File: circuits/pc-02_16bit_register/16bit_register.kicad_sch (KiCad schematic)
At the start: 34 parts, among them J1 Conn_01x10, U1 74HC273, U2 74HC273, U3 74HC244, U4 74HC244, U5 74HC244, U6 74HC244

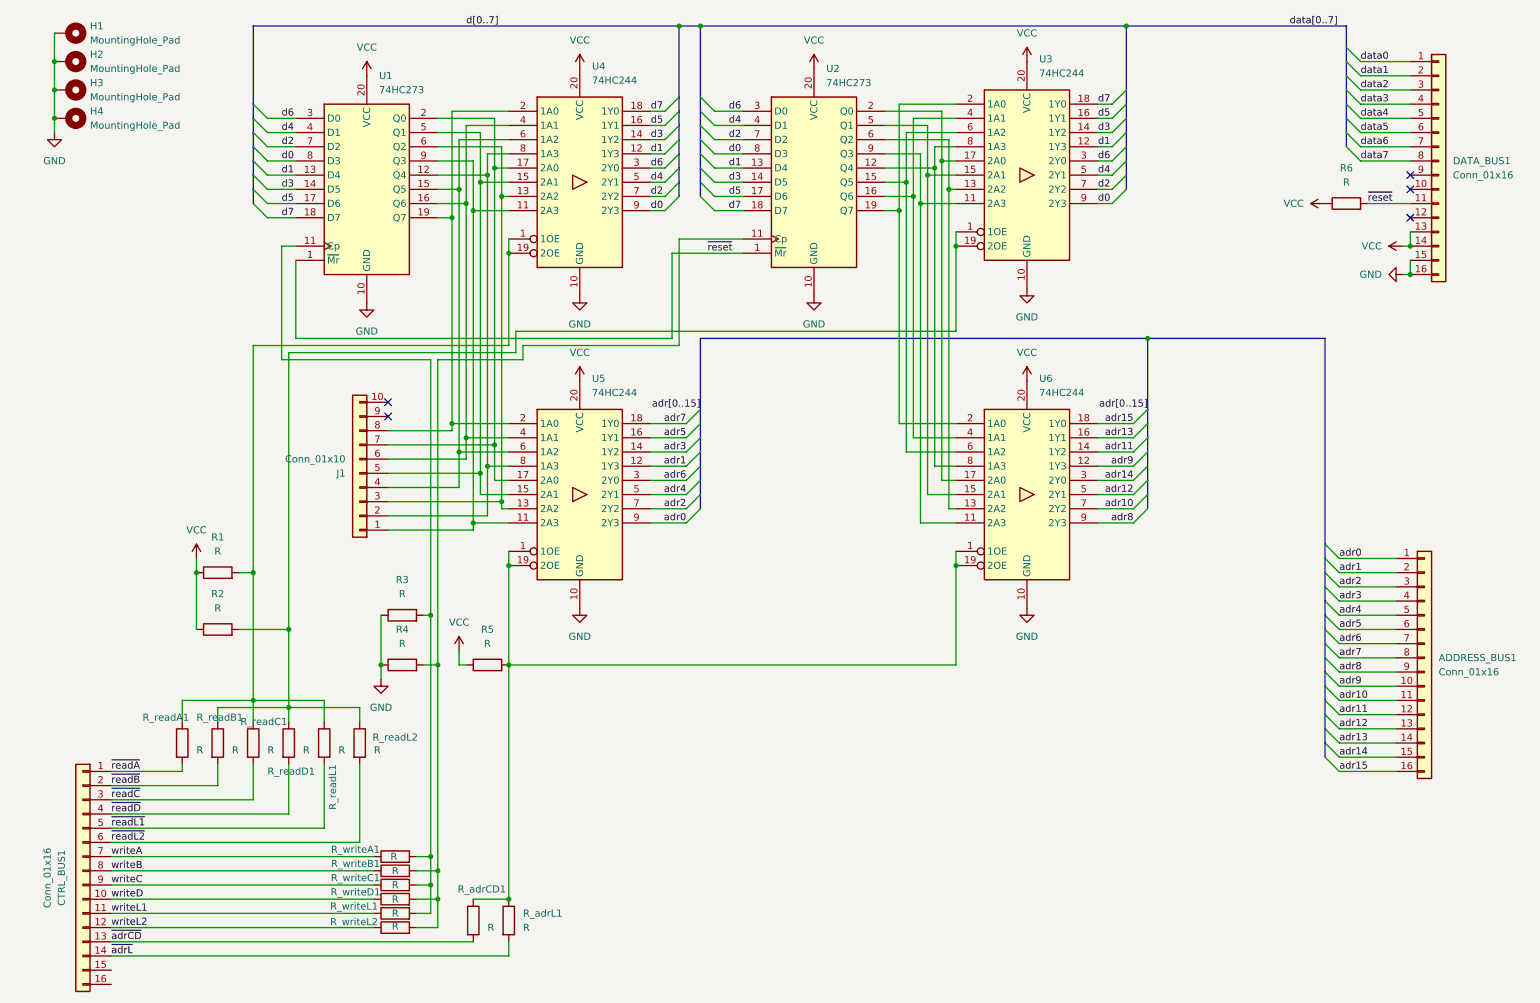
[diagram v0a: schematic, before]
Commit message: pc-02 rev A: 16bit register unit for PC and SP
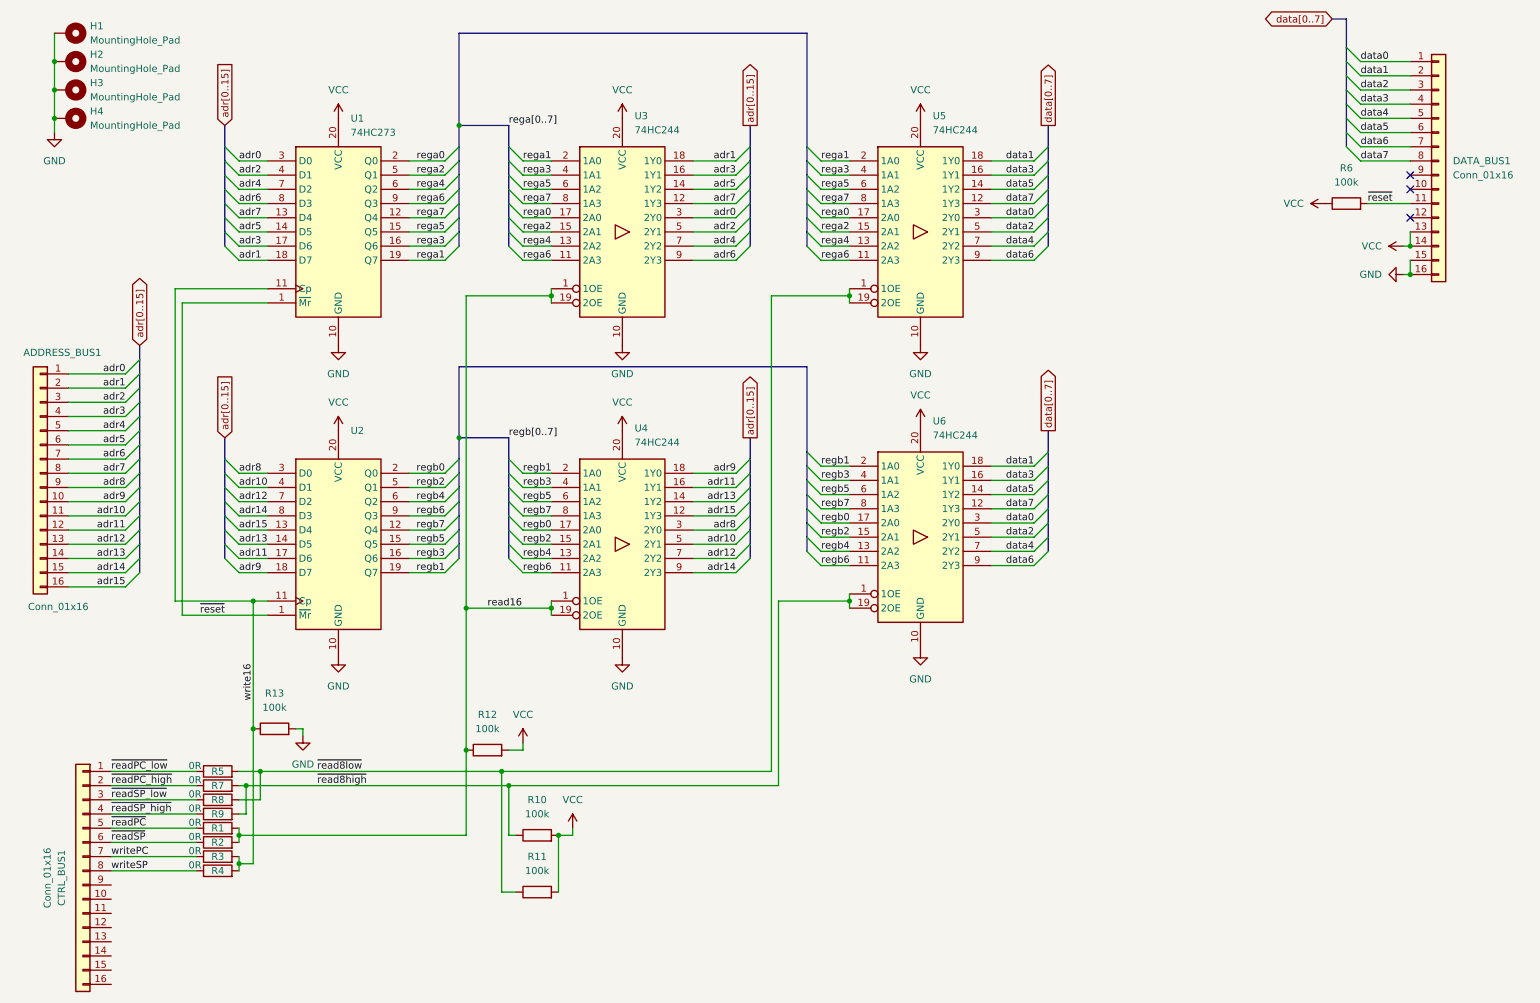
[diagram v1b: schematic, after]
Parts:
- removed J1: Conn_01x10, Connector_IDC:IDC-Header_2x05_P2.54mm_Horizontal, symbol Connector_Generic:Conn_01x10
- removed R_adrCD1, R_adrL1, R_readA1, R_readB1, R_readC1, R_readD1, R_readL1, R_readL2, R_writeA1, R_writeB1, R_writeC1, R_writeD1, R_writeL1, R_writeL2: R, Resistor_SMD:R_0603_1608Metric, symbol Device:R
- added R10, R11, R12, R13: 100k, Resistor_SMD:R_0603_1608Metric, symbol Device:R
- added R7, R8, R9: 0R, Resistor_SMD:R_0603_1608Metric, symbol Device:R
- R1, R2, R3, R4, R5: value R -> 0R
- R6: value R -> 100k
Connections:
- net GND: now also R13.2; no longer R3.1, R4.1
- net VCC: now also R10.2, R11.2, R12.2; no longer R1.1, R2.1, R5.1
- net adr0: now also U1.3 (D0), U3.3 (2Y0); no longer U5.9 (2Y3)
- net adr1: now also U1.18 (D7), U3.18 (1Y0); no longer U5.12 (1Y3)
- net adr10: now also U2.4 (D1), U4.5 (2Y1); no longer U6.7 (2Y2)
- net adr11: now also U2.17 (D6), U4.16 (1Y1); no longer U6.14 (1Y2)
- net adr12: now also U2.7 (D2), U4.7 (2Y2); no longer U6.5 (2Y1)
- net adr13: now also U2.14 (D5), U4.14 (1Y2); no longer U6.16 (1Y1)
- net adr14: now also U2.8 (D3), U4.9 (2Y3); no longer U6.3 (2Y0)
- net adr15: now also U2.13 (D4), U4.12 (1Y3); no longer U6.18 (1Y0)
- net adr2: now also U1.4 (D1), U3.5 (2Y1); no longer U5.7 (2Y2)
- net adr3: now also U1.17 (D6), U3.16 (1Y1); no longer U5.14 (1Y2)
- net adr4: now also U1.7 (D2), U3.7 (2Y2); no longer U5.5 (2Y1)
- net adr5: now also U1.14 (D5), U3.14 (1Y2); no longer U5.16 (1Y1)
- net adr6: now also U1.8 (D3), U3.9 (2Y3); no longer U5.3 (2Y0)
- net adr7: now also U1.13 (D4), U3.12 (1Y3); no longer U5.18 (1Y0)
- net adr8: now also U2.3 (D0), U4.3 (2Y0); no longer U6.9 (2Y3)
- net adr9: now also U2.18 (D7), U4.18 (1Y0); no longer U6.12 (1Y3)
- net data0: now also U5.3 (2Y0), U6.3 (2Y0)
- net data1: now also U5.18 (1Y0), U6.18 (1Y0)
- net data2: now also U5.5 (2Y1), U6.5 (2Y1)
- net data3: now also U5.16 (1Y1), U6.16 (1Y1)
- net data4: now also U5.7 (2Y2), U6.7 (2Y2)
- net data5: now also U5.14 (1Y2), U6.14 (1Y2)
- net data6: now also U5.9 (2Y3), U6.9 (2Y3)
- net data7: now also U5.12 (1Y3), U6.12 (1Y3)
- net write16: now reaches R3.2, U1.11 (Cp)
- net write16: now also R4.2, U2.11 (Cp), R13.1
- net rega7: now reaches U1.12 (Q4), U5.8 (1A3)
- net rega7: now also U3.8 (1A3); no longer U4.8 (1A3)
- net rega5: now reaches U1.15 (Q5), U5.6 (1A2)
- net rega5: now also U3.6 (1A2); no longer U4.6 (1A2)
- net rega3: now reaches U1.16 (Q6), U5.4 (1A1)
- net rega3: now also U3.4 (1A1); no longer U4.4 (1A1)
- net rega1: now reaches U1.19 (Q7), U5.2 (1A0)
- net rega1: now also U3.2 (1A0); no longer U4.2 (1A0)
- net rega0: now reaches U1.2 (Q0), U5.17 (2A0)
- net rega0: now also U3.17 (2A0); no longer U4.17 (2A0)
- net rega2: now reaches U1.5 (Q1), U5.15 (2A1)
- net rega2: now also U3.15 (2A1); no longer U4.15 (2A1)
- net rega4: now reaches U1.6 (Q2), U5.13 (2A2)
- net rega4: now also U3.13 (2A2); no longer U4.13 (2A2)
- net rega6: now reaches U1.9 (Q3), U5.11 (2A3)
- net rega6: now also U3.11 (2A3); no longer U4.11 (2A3)
- net ~{read8low}: now reaches R5.2, U5.1 (1OE), U5.19 (2OE)
- net ~{read8low}: now also R11.1, R8.2; no longer U6.1 (1OE), U6.19 (2OE)
- net read16: now reaches R2.2, U3.1 (1OE), U3.19 (2OE)
- net read16: now also R1.2, U4.1 (1OE), U4.19 (2OE), R12.1
- net regb7: now reaches U2.12 (Q4), U6.8 (1A3)
- net regb7: now also U4.8 (1A3); no longer U3.8 (1A3)
- net regb5: now reaches U2.15 (Q5), U6.6 (1A2)
- net regb5: now also U4.6 (1A2); no longer U3.6 (1A2)
- net regb3: now reaches U2.16 (Q6), U6.4 (1A1)
- net regb3: now also U4.4 (1A1); no longer U3.4 (1A1)
- net regb1: now reaches U2.19 (Q7), U6.2 (1A0)
- net regb1: now also U4.2 (1A0); no longer U3.2 (1A0)
- net regb0: now reaches U2.2 (Q0), U6.17 (2A0)
- net regb0: now also U4.17 (2A0); no longer U3.17 (2A0)
- net regb2: now reaches U2.5 (Q1), U6.15 (2A1)
- net regb2: now also U4.15 (2A1); no longer U3.15 (2A1)
- net regb4: now reaches U2.6 (Q2), U6.13 (2A2)
- net regb4: now also U4.13 (2A2); no longer U3.13 (2A2)
- net regb6: now reaches U2.9 (Q3), U6.11 (2A3)
- net regb6: now also U4.11 (2A3); no longer U3.11 (2A3)
- removed net d0: U1.8 (D3), U2.8 (D3), U3.9 (2Y3), U4.9 (2Y3)
- removed net d1: U1.13 (D4), U2.13 (D4), U3.12 (1Y3), U4.12 (1Y3)
- removed net d2: U1.7 (D2), U2.7 (D2), U3.7 (2Y2), U4.7 (2Y2)
- removed net d3: U1.14 (D5), U2.14 (D5), U3.14 (1Y2), U4.14 (1Y2)
- removed net d4: U1.4 (D1), U2.4 (D1), U3.5 (2Y1), U4.5 (2Y1)
- removed net d5: U1.17 (D6), U2.17 (D6), U3.16 (1Y1), U4.16 (1Y1)
- removed net d6: U1.3 (D0), U2.3 (D0), U3.3 (2Y0), U4.3 (2Y0)
- removed net d7: U1.18 (D7), U2.18 (D7), U3.18 (1Y0), U4.18 (1Y0)
- net writeA renamed writePC
- net writePC: now also R3.1
- net writeB renamed writeSP
- net writeSP: now also R4.1
- net writeC: no longer names the net of CTRL_BUS1.9 (Pin_9)
- net writeD: no longer names the net of CTRL_BUS1.10 (Pin_10)
- net writeL1: no longer names the net of CTRL_BUS1.11 (Pin_11)
- net writeL2: no longer names the net of CTRL_BUS1.12 (Pin_12)
- net ~{adrCD}: no longer names the net of CTRL_BUS1.13 (Pin_13)
- net ~{adrL}: no longer names the net of CTRL_BUS1.14 (Pin_14)
- net ~{readA} renamed ~{readPC_low}
- net ~{readPC_low}: now also R5.1
- net ~{readB} renamed ~{readPC_high}
- net ~{readPC_high}: now also R7.1
- net ~{readC} renamed ~{readSP_low}
- net ~{readSP_low}: now also R8.1
- net ~{readD} renamed ~{readSP_high}
- net ~{readSP_high}: now also R9.1
- net ~{readL1} renamed ~{readPC}
- net ~{readPC}: now also R1.1
- net ~{readL2} renamed ~{readSP}
- net ~{readSP}: now also R2.1
- new net ~{read8high}: R10.1, R7.2, R9.2, U6.1 (1OE), U6.19 (2OE)
- no-connect marks 5 -> 3
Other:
- title: PC-01 Dual Register Unit -> PC-02 16Bit Register Unit
- moved on the sheet: ADDRESS_BUS1, U1, U2, U3, U4, U5, U6

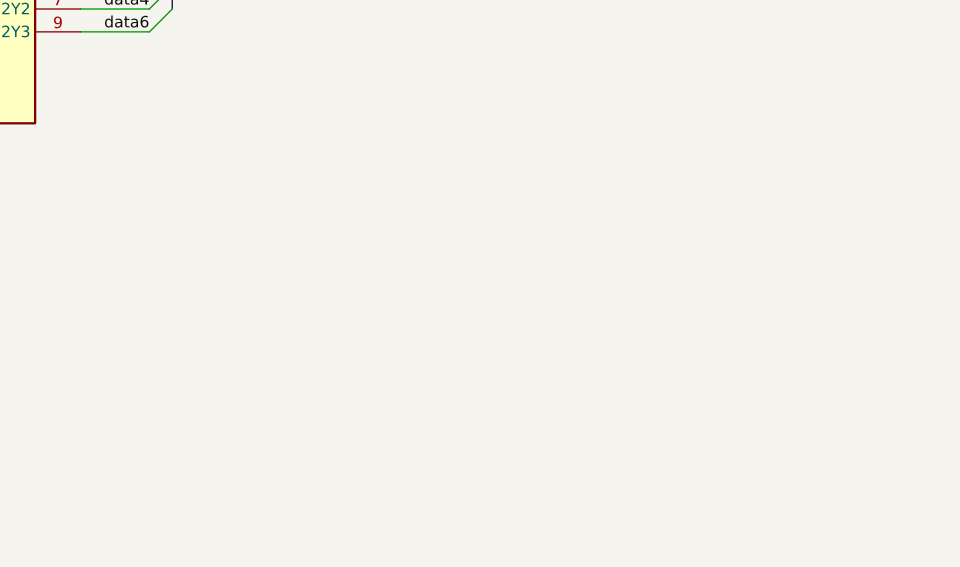
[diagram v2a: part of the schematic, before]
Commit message: add filter and decoupling capacitors to all boards
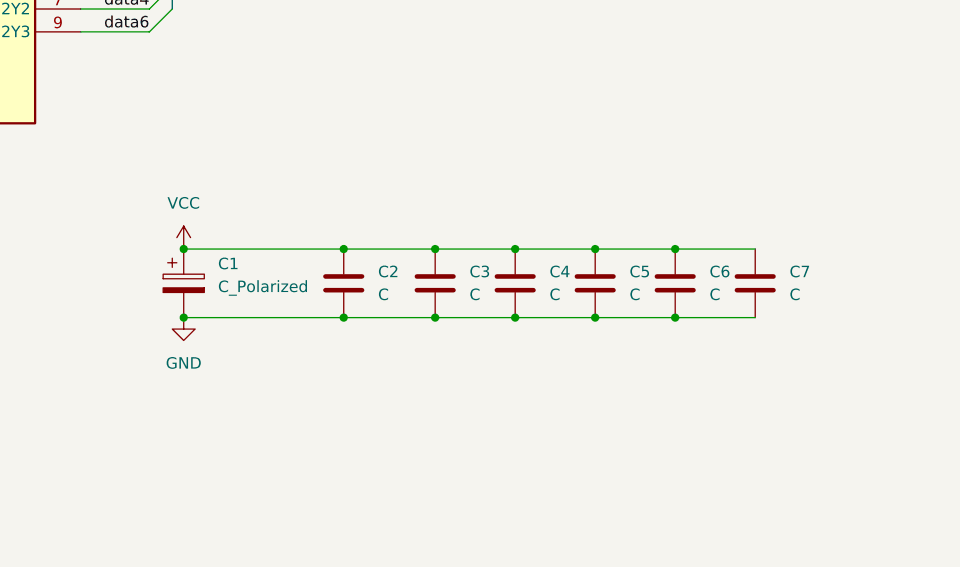
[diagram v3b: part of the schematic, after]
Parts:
- added C1: C_Polarized, Capacitor_SMD:CP_Elec_5x5.3, symbol Device:C_Polarized
- added C2, C3, C4, C5, C6, C7: C, Capacitor_SMD:C_0603_1608Metric, symbol Device:C
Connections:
- net GND: now also C1.2, C2.2, C3.2, C4.2, C5.2, C6.2, C7.2
- net VCC: now also C1.1, C2.1, C3.1, C4.1, C5.1, C6.1, C7.1

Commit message: pcb design
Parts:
- added R14, R15, R16: 0R, Resistor_SMD:R_0603_1608Metric, symbol Device:R
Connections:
- net write16: now also R14.2
- net ~{read8high}: now also R16.2
- net ~{read8low}: now also R15.2
- net writeIPC: now reaches CTRL_BUS1.12 (Pin_12)
- net writeIPC: now also R14.1
- net ~{readIPC_low}: now reaches CTRL_BUS1.13 (Pin_13)
- net ~{readIPC_low}: now also R15.1
- net ~{readIPC_high}: now reaches CTRL_BUS1.14 (Pin_14)
- net ~{readIPC_high}: now also R16.1
- no-connect marks 3 -> 8
